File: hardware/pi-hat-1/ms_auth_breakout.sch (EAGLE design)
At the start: 38 parts, among them IC1 ULN2003AD, J11 BUCK_MODULEHORIZONTAL, J9 POWER_JACKPTH_LOCK, Q1 DMN3023L, Q2 DMN3023L, Q3 DMN3023L, Q4 DMN3023L, Q5 DMN3023L, Q6 DMN3023L

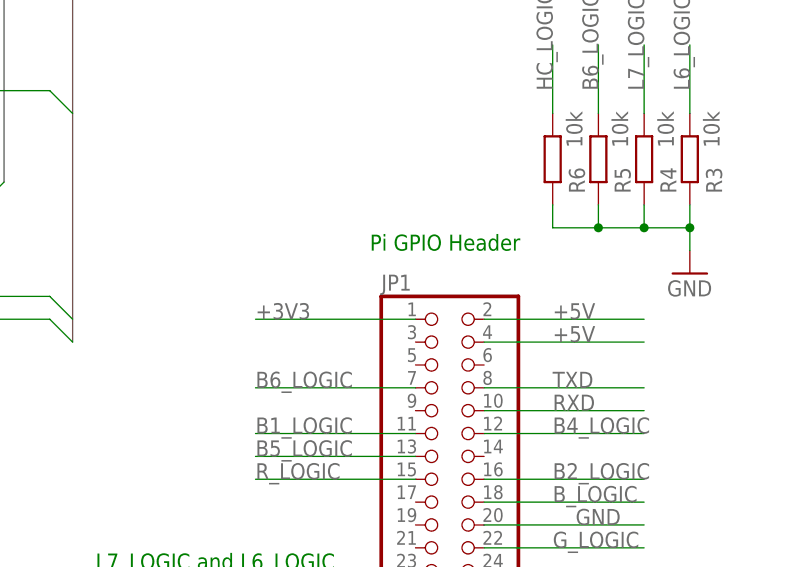
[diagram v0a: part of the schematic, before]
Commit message: Rename JP1->J14, move some vias
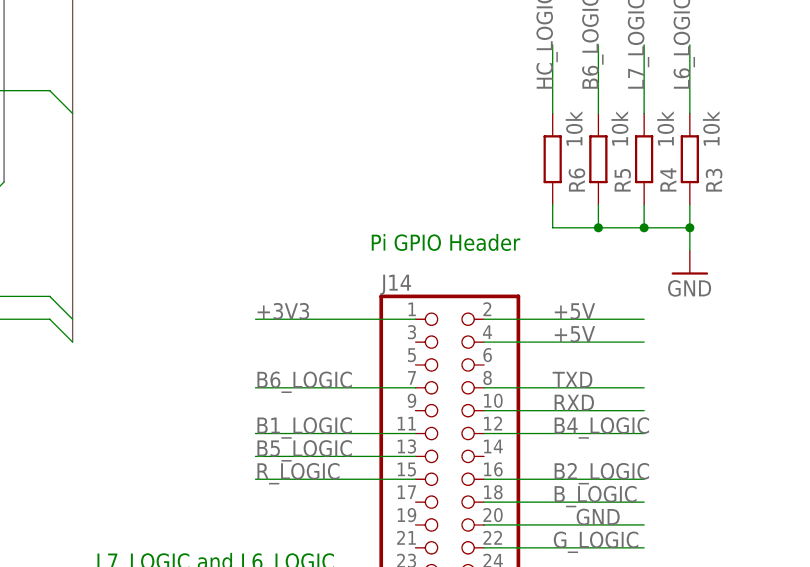
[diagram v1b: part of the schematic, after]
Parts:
- renumbered JP1 to J14
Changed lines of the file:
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@@
 <parts>
 <part name="FRAME1" library="frames" deviceset="LETTER_L" device=""/>
-<part name="JP1" library="pinhead" deviceset="PINHD-2X20" device=""/>
+<part name="J14" library="pinhead" deviceset="PINHD-2X20" device=""/>
 <part name="IC1" library="uln-udn" deviceset="ULN2003A" device="D"/>
 <part name="P+1" library="supply1" deviceset="+12V" device=""/>
@@
 <instance part="FRAME1" gate="G$1" x="0" y="0"/>
 <instance part="FRAME1" gate="G$2" x="147.32" y="0"/>
-<instance part="JP1" gate="A" x="99.06" y="40.64"/>
+<instance part="J14" gate="A" x="99.06" y="40.64"/>
 <instance part="IC1" gate="A" x="93.98" y="121.92"/>
 <instance part="P+1" gate="1" x="185.42" y="86.36"/>
@@
 </segment>
 <segment>
-<pinref part="JP1" gate="A" pin="20"/>
+<pinref part="J14" gate="A" pin="20"/>
 <wire x1="104.14" y1="40.64" x2="121.92" y2="40.64" width="0.1524" layer="91"/>
 <label x="114.3" y="40.64" size="1.778" layer="95"/>
 </segment>
 <segment>
-<pinref part="JP1" gate="A" pin="34"/>
+<pinref part="J14" gate="A" pin="34"/>
 <wire x1="104.14" y1="22.86" x2="121.92" y2="22.86" width="0.1524" layer="91"/>
 <label x="114.3" y="22.86" size="1.778" layer="95"/>
 </segment>
 <segment>
-<pinref part="JP1" gate="A" pin="39"/>
+<pinref part="J14" gate="A" pin="39"/>
 <wire x1="96.52" y1="15.24" x2="78.74" y2="15.24" width="0.1524" layer="91"/>
 <label x="81.28" y="15.24" size="1.778" layer="95"/>
@@
 <net name="TXD" class="0">
 <segment>
-<pinref part="JP1" gate="A" pin="8"/>
+<pinref part="J14" gate="A" pin="8"/>
 <wire x1="104.14" y1="55.88" x2="121.92" y2="55.88" width="0.1524" layer="91"/>
 <label x="111.76" y="55.88" size="1.778" layer="95"/>
@@
 <net name="RXD" class="0">
 <segment>
-<pinref part="JP1" gate="A" pin="10"/>
+<pinref part="J14" gate="A" pin="10"/>
 <wire x1="104.14" y1="53.34" x2="121.92" y2="53.34" width="0.1524" layer="91"/>
 <label x="111.76" y="53.34" size="1.778" layer="95"/>
@@
 <net name="+3V3" class="0">
 <segment>
-<pinref part="JP1" gate="A" pin="1"/>
+<pinref part="J14" gate="A" pin="1"/>
 <wire x1="96.52" y1="63.5" x2="78.74" y2="63.5" width="0.1524" layer="91"/>
 <label x="78.74" y="63.5" size="1.778" layer="95"/>
@@
 </segment>
 <segment>
-<pinref part="JP1" gate="A" pin="11"/>
+<pinref part="J14" gate="A" pin="11"/>
 <wire x1="96.52" y1="50.8" x2="78.74" y2="50.8" width="0.1524" layer="91"/>
 <label x="78.74" y="50.8" size="1.778" layer="95"/>
@@
 </segment>
 <segment>
-<pinref part="JP1" gate="A" pin="16"/>
+<pinref part="J14" gate="A" pin="16"/>
 <wire x1="104.14" y1="45.72" x2="121.92" y2="45.72" width="0.1524" layer="91"/>
 <label x="111.76" y="45.72" size="1.778" layer="95"/>
@@
 </segment>
 <segment>
-<pinref part="JP1" gate="A" pin="33"/>
+<pinref part="J14" gate="A" pin="33"/>
 <wire x1="96.52" y1="22.86" x2="78.74" y2="22.86" width="0.1524" layer="91"/>
 <label x="78.74" y="22.86" size="1.778" layer="95"/>
@@
 </segment>
 <segment>
-<pinref part="JP1" gate="A" pin="35"/>
+<pinref part="J14" gate="A" pin="35"/>
 <wire x1="78.74" y1="20.32" x2="96.52" y2="20.32" width="0.1524" layer="91"/>
 <label x="78.74" y="20.32" size="1.778" layer="95"/>
@@
 </segment>
 <segment>
-<pinref part="JP1" gate="A" pin="36"/>
+<pinref part="J14" gate="A" pin="36"/>
 <wire x1="104.14" y1="20.32" x2="121.92" y2="20.32" width="0.1524" layer="91"/>
 <label x="111.76" y="20.32" size="1.778" layer="95"/>
@@
 </segment>
 <segment>
-<pinref part="JP1" gate="A" pin="37"/>
+<pinref part="J14" gate="A" pin="37"/>
 <wire x1="96.52" y1="17.78" x2="78.74" y2="17.78" width="0.1524" layer="91"/>
 <label x="78.74" y="17.78" size="1.778" layer="95"/>
@@
 </segment>
 <segment>
-<pinref part="JP1" gate="A" pin="38"/>
+<pinref part="J14" gate="A" pin="38"/>
 <wire x1="121.92" y1="17.78" x2="104.14" y2="17.78" width="0.1524" layer="91"/>
 <label x="111.76" y="17.78" size="1.778" layer="95"/>
@@
 </segment>
 <segment>
-<pinref part="JP1" gate="A" pin="32"/>
+<pinref part="J14" gate="A" pin="32"/>
 <wire x1="104.14" y1="25.4" x2="121.92" y2="25.4" width="0.1524" layer="91"/>
 <label x="111.76" y="25.4" size="1.778" layer="95"/>
@@
 </segment>
 <segment>
-<pinref part="JP1" gate="A" pin="12"/>
+<pinref part="J14" gate="A" pin="12"/>
 <wire x1="104.14" y1="50.8" x2="121.92" y2="50.8" width="0.1524" layer="91"/>
 <label x="111.76" y="50.8" size="1.778" layer="95"/>
@@
 </segment>
 <segment>
-<pinref part="JP1" gate="A" pin="13"/>
+<pinref part="J14" gate="A" pin="13"/>
 <wire x1="78.74" y1="48.26" x2="96.52" y2="48.26" width="0.1524" layer="91"/>
 <label x="78.74" y="48.26" size="1.778" layer="95"/>
@@
 </segment>
 <segment>
-<pinref part="JP1" gate="A" pin="2"/>
+<pinref part="J14" gate="A" pin="2"/>
 <wire x1="104.14" y1="63.5" x2="121.92" y2="63.5" width="0.1524" layer="91"/>
 <label x="111.76" y="63.5" size="1.778" layer="95"/>
 </segment>
 <segment>
-<pinref part="JP1" gate="A" pin="4"/>
+<pinref part="J14" gate="A" pin="4"/>
 <wire x1="104.14" y1="60.96" x2="121.92" y2="60.96" width="0.1524" layer="91"/>
 <label x="111.76" y="60.96" size="1.778" layer="95"/>
@@
 </segment>
 <segment>
-<pinref part="JP1" gate="A" pin="31"/>
+<pinref part="J14" gate="A" pin="31"/>
 <wire x1="78.74" y1="25.4" x2="96.52" y2="25.4" width="0.1524" layer="91"/>
 <label x="78.74" y="25.4" size="1.778" layer="95"/>
@@
 <net name="L7_LOGIC" class="0">
 <segment>
-<pinref part="JP1" gate="A" pin="29"/>
+<pinref part="J14" gate="A" pin="29"/>
 <wire x1="96.52" y1="27.94" x2="78.74" y2="27.94" width="0.1524" layer="91"/>
 <label x="78.74" y="27.94" size="1.778" layer="95"/>
@@
 </segment>
 <segment>
-<pinref part="JP1" gate="A" pin="15"/>
+<pinref part="J14" gate="A" pin="15"/>
 <wire x1="96.52" y1="45.72" x2="78.74" y2="45.72" width="0.1524" layer="91"/>
 <label x="78.74" y="45.72" size="1.778" layer="95"/>
@@
 </segment>
 <segment>
-<pinref part="JP1" gate="A" pin="22"/>
+<pinref part="J14" gate="A" pin="22"/>
 <wire x1="104.14" y1="38.1" x2="121.92" y2="38.1" width="0.1524" layer="91"/>
 <label x="111.76" y="38.1" size="1.778" layer="95"/>
@@
 </segment>
 <segment>
-<pinref part="JP1" gate="A" pin="18"/>
+<pinref part="J14" gate="A" pin="18"/>
 <wire x1="104.14" y1="43.18" x2="121.92" y2="43.18" width="0.1524" layer="91"/>
 <label x="111.76" y="43.18" size="1.778" layer="95"/>
@@
 <net name="B6_LOGIC" class="0">
 <segment>
-<pinref part="JP1" gate="A" pin="7"/>
+<pinref part="J14" gate="A" pin="7"/>
 <wire x1="96.52" y1="55.88" x2="78.74" y2="55.88" width="0.1524" layer="91"/>
 <label x="78.74" y="55.88" size="1.778" layer="95"/>
@@
 <net name="HC_LOGIC" class="0">
 <segment>
-<pinref part="JP1" gate="A" pin="40"/>
+<pinref part="J14" gate="A" pin="40"/>
 <wire x1="104.14" y1="15.24" x2="121.92" y2="15.24" width="0.1524" layer="91"/>
 <label x="114.3" y="15.24" size="1.778" layer="95"/>
